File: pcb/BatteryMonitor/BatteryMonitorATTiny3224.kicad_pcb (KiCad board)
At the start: 2 copper layers, 56.7 x 25.4 mm, 26 parts, among them IC101 MAX3485E, IC102 ATTINY3224-SS, P101 RS485, P102 Bat, P103 Prog, U101 AMS1117, U103 MAX9918

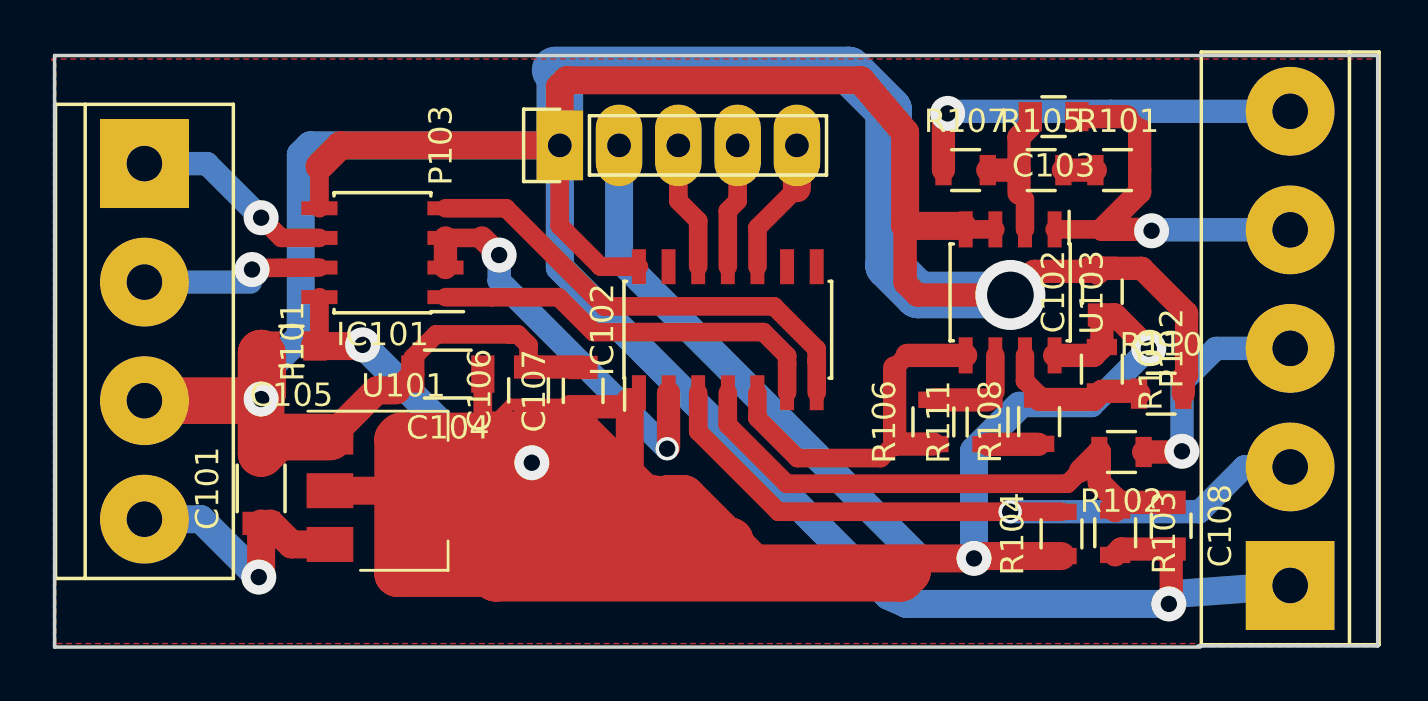
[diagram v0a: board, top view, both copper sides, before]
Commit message: Eliminated current Amp, using only Attiny3224 ADC
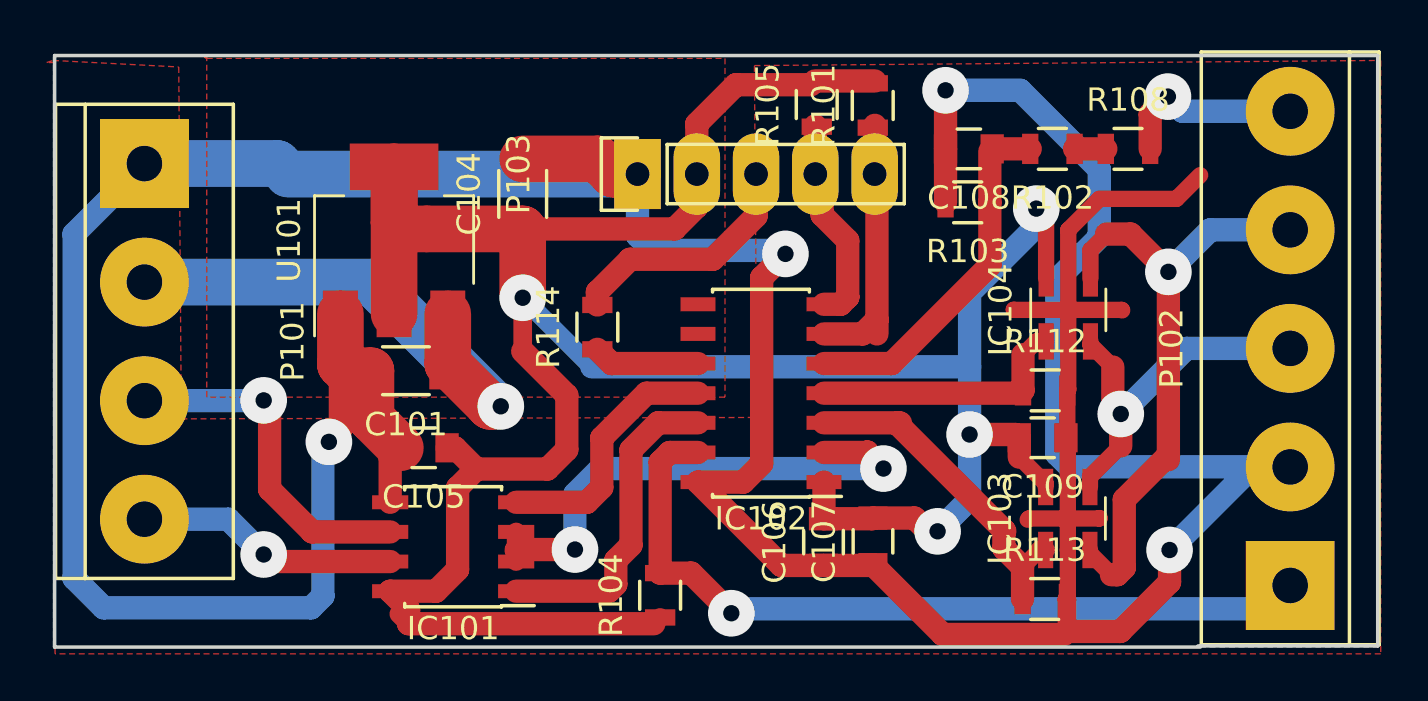
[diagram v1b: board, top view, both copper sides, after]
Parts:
- removed C102: 100nF, Capacitors_SMD:C_0805
- removed C103: 10nF, Capacitors_SMD:C_0805
- removed R106, R107, R109, R110: 100K, Resistors_SMD:R_0805
- removed R111: 1K, Resistors_SMD:R_0805
- removed U103: MAX9918, Housings_SOIC:SOIC-8_3.9x4.9mm_Pitch1.27mm
- added C109: 100nF, Capacitors_SMD:C_0805, F.Cu at (151.5, 60.5)
- added IC103: INA169, TO_SOT_Packages_SMD:SOT-23-5_HandSoldering, F.Cu at (152.6, 64.0)
- added IC104: INA169, TO_SOT_Packages_SMD:SOT-23-5_HandSoldering, F.Cu at (152.6, 55.0)
- added R112: 47K, Resistors_SMD:R_0805, F.Cu at (151.6, 58.5)
- added R113: 47K, Resistors_SMD:R_0805, F.Cu at (151.6, 67.4)
- added R114: 270R, Resistors_SMD:R_0805, F.Cu at (132.4, 55.8)
- R101, R105: value 100K -> 10K
- R108: value 100R -> 10K
- moved C108 18.3 mm to (148.3, 48.1), turned to 180 degrees
- moved R104 17.4 mm to (135.1, 67.3)
- moved R103 15.5 mm to (148.3, 50.4), turned to 180 degrees
- moved C106 14.2 mm to (142.1, 65.0)
- moved C107 14.0 mm to (144.2, 65.0)
- moved R102 13.3 mm to (151.9, 48.1)
- moved IC101 13.0 mm to (126.2, 65.2)
- moved R108 12.3 mm to (155.2, 48.1), turned to 0 degrees
- moved R101 10.8 mm to (144.2, 46.3), turned to 90 degrees
- moved U101 10.7 mm to (123.7, 52.1), turned to 90 degrees
- moved R105 10.0 mm to (141.8, 46.2), turned to 90 degrees
- moved C104 8.36 mm to (129.2, 50.1), turned to 90 degrees
- moved C101 8.00 mm to (124.2, 57.7), turned to 180 degrees
- moved C105 7.15 mm to (125.0, 61.0)
- moved P103 3.55 mm to (134.1, 49.2)
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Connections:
- C106 pad 1: 5v -> GND
- C106 pad 2: GND -> 5v
- C107 pad 1: 5v -> GND
- C107 pad 2: GND -> 5v
- IC102 pad 10: UDPI -> Net-(IC102-Pad10)
- IC102 pad 11: TXDebug -> TX
- IC102 pad 12: RXDebug -> RX
- IC102 pad 13: (no net) -> NTC
- IC102 pad 3: NTC -> Sense-
- IC102 pad 4: BatSenseV -> CurSenseV
- IC102 pad 5: CurSenseV -> BatSenseV
- IC102 pad 6: RX -> RXDebug
- IC102 pad 7: TX -> TXDebug
- P101 pad 1: RS485-A -> GND
- P101 pad 2: RS485-B -> Vin
- P101 pad 3: GND -> RS485-A
- P101 pad 4: Vin -> RS485-B
- P102 pad 1: GND -> NTC
- P102 pad 2: NTC -> GND
- P102 pad 3: BatV+ -> RS+
- P102 pad 4: RS+ -> RS-
- P102 pad 5: RS- -> BatV+
- P103 pad 3: RXDebug -> UDPI
- P103 pad 5: UDPI -> RXDebug
- R101 pad 1: Net-(R101-Pad1) -> RXDebug
- R101 pad 2: RS+ -> 5v
- R102 pad 1: BatV+ -> Net-(R102-Pad1)
- R105 pad 1: Net-(C103-Pad2) -> TXDebug
- R105 pad 2: Net-(R101-Pad1) -> 5v
- R108 pad 1: Net-(R108-Pad1) -> Net-(R102-Pad1)
- R108 pad 2: Net-(R108-Pad2) -> BatV+
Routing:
- net 5v: track 198.3 -> 125.2 mm
- net Sense-: track 0.00 -> 14.7 mm
- net Vin: track 11.6 -> 24.0 mm
- net RS-: track 17.5 -> 27.3 mm
- net TX: track 20.3 -> 11.0 mm
- net BatSenseV: track 24.4 -> 15.5 mm
- net GND: track 205.8 -> 198.6 mm, vias 3 -> 4
- net Net-(R108-Pad2): track 6.61 -> 0.00 mm
- net Net-(C103-Pad2): track 6.47 -> 0.00 mm
- net RS485-A: track 8.82 -> 15.0 mm
- net RXDebug: track 5.55 -> 11.6 mm
- net TXEN: track 17.6 -> 22.8 mm
- net RX: track 18.4 -> 13.8 mm
- net CurSenseV: track 16.1 -> 11.5 mm
- net UDPI: track 5.90 -> 10.5 mm
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- added copper zone on F.Cu, net 5v
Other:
- net class Default: clearance 0.3 -> 0.2; trace_width 2 -> 0.7; via_dia 3 -> 2; via_drill 2 -> 0.7
- rule trace_clearance: 0.3 -> 0.2
